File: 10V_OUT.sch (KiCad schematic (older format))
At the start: 7 parts, among them U1 LM321

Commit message: Comments and Notation for clarity
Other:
- note added: "2nd Order Low Pass Filter"
- note added: "Non-Inverting Amplifier"
- moved on the sheet: R3, R4, U1
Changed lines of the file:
@@
 L Amplifier_Operational:LM321 U1
 U 1 1 60A73539
-P 6850 3450
-F 0 "U1" H 7194 3496 50  0000 L CNN
-F 1 "LM321" H 7194 3405 50  0000 L CNN
-F 2 "Package_TO_SOT_SMD:SOT-23-5" H 6850 3450 50  0001 C CNN
-F 3 "http://www.ti.com/lit/ds/symlink/lm321.pdf" H 6850 3450 50  0001 C CNN
-	1    6850 3450
+P 7150 3450
+F 0 "U1" H 7250 3350 50  0000 L CNN
+F 1 "LM321" H 7250 3250 50  0000 L CNN
+F 2 "Package_TO_SOT_SMD:SOT-23-5" H 7150 3450 50  0001 C CNN
+F 3 "http://www.ti.com/lit/ds/symlink/lm321.pdf" H 7150 3450 50  0001 C CNN
+	1    7150 3450
 	1    0    0    -1
 $EndComp
@@
 L Device:R_US R4
 U 1 1 60A77E98
-P 6800 4350
-F 0 "R4" V 6595 4350 50  0000 C CNN
-F 1 "22k" V 6686 4350 50  0000 C CNN
-F 2 "" V 6840 4340 50  0001 C CNN
-F 3 "~" H 6800 4350 50  0001 C CNN
-	1    6800 4350
+P 7100 4350
+F 0 "R4" V 6895 4350 50  0000 C CNN
+F 1 "22k" V 6986 4350 50  0000 C CNN
+F 2 "" V 7140 4340 50  0001 C CNN
+F 3 "~" H 7100 4350 50  0001 C CNN
+	1    7100 4350
 	0    1    1    0
 $EndComp
@@
 L Device:R_US R3
 U 1 1 60A78F26
-P 6300 4350
-F 0 "R3" V 6095 4350 50  0000 C CNN
-F 1 "10k" V 6186 4350 50  0000 C CNN
-F 2 "" V 6340 4340 50  0001 C CNN
-F 3 "~" H 6300 4350 50  0001 C CNN
-	1    6300 4350
+P 6600 4350
+F 0 "R3" V 6395 4350 50  0000 C CNN
+F 1 "10k" V 6486 4350 50  0000 C CNN
+F 2 "" V 6640 4340 50  0001 C CNN
+F 3 "~" H 6600 4350 50  0001 C CNN
+	1    6600 4350
 	0    1    1    0
 $EndComp
@@
 	5950 3350 5950 3550
 Wire Wire Line
-	5950 3350 6550 3350
-Connection ~ 5950 3350
+	7450 3450 7600 3450
 Wire Wire Line
-	7150 3450 7300 3450
+	7600 3450 7600 4350
 Wire Wire Line
-	7300 3450 7300 4350
+	7600 4350 7250 4350
 Wire Wire Line
-	7300 4350 6950 4350
+	6950 4350 6850 4350
 Wire Wire Line
-	6650 4350 6550 4350
+	6850 3550 6850 4350
+Connection ~ 6850 4350
 Wire Wire Line
-	6550 3550 6550 4350
-Connection ~ 6550 4350
-Wire Wire Line
-	6550 4350 6450 4350
-Wire Wire Line
-	6150 4350 5950 4350
+	6850 4350 6750 4350
 Wire Wire Line
 	5250 4050 5250 4350
@@
 Wire Wire Line
 	5950 4050 5950 4350
+Wire Wire Line
+	5950 4350 5250 4350
+Text HLabel 7950 3450 2    50   Input ~ 0
+OUT
+Wire Wire Line
+	7600 3450 7950 3450
+Connection ~ 7600 3450
+Text GLabel 7250 3900 2    50   Input ~ 0
+GND
+Wire Wire Line
+	7050 3750 7050 3900
+Wire Wire Line
+	7050 3900 7250 3900
+Text GLabel 7250 3000 2    50   Input ~ 0
+24V
+Wire Wire Line
+	7050 3150 7050 3000
+Wire Wire Line
+	7050 3000 7250 3000
+Wire Wire Line
+	5950 4350 6450 4350
 Connection ~ 5950 4350
 Wire Wire Line
-	5950 4350 5250 4350
-Text HLabel 7650 3450 2    50   Input ~ 0
-OUT
-Wire Wire Line
-	7300 3450 7650 3450
-Connection ~ 7300 3450
-Text GLabel 6950 3900 2    50   Input ~ 0
-GND
-Wire Wire Line
-	6750 3750 6750 3900
-Wire Wire Line
-	6750 3900 6950 3900
-Text GLabel 6950 3000 2    50   Input ~ 0
-24V
-Wire Wire Line
-	6750 3150 6750 3000
-Wire Wire Line
-	6750 3000 6950 3000
+	6850 3350 5950 3350
+Connection ~ 5950 3350
+Wire Notes Line
+	4650 3100 6400 3100
+Wire Notes Line
+	6400 3100 6400 4450
+Wire Notes Line
+	6400 4450 4650 4450
+Wire Notes Line
+	4650 4450 4650 3100
+Text Notes 5050 4550 0    50   ~ 0
+2nd Order Low Pass Filter
+Wire Notes Line
+	6450 2900 7750 2900
+Wire Notes Line
+	7750 2900 7750 4450
+Wire Notes Line
+	7750 4450 6450 4450
+Wire Notes Line
+	6450 4450 6450 2900
+Text Notes 6650 4550 0    50   ~ 0
+Non-Inverting Amplifier
 $EndSCHEMATC

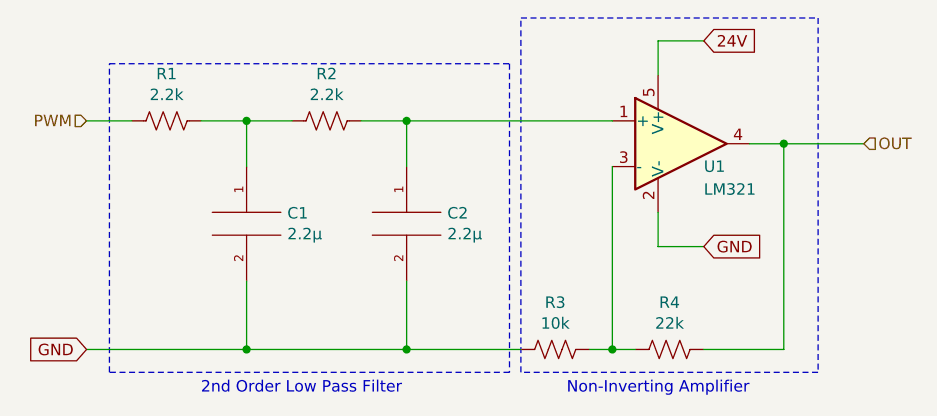
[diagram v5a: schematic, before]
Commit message: Footprint Association
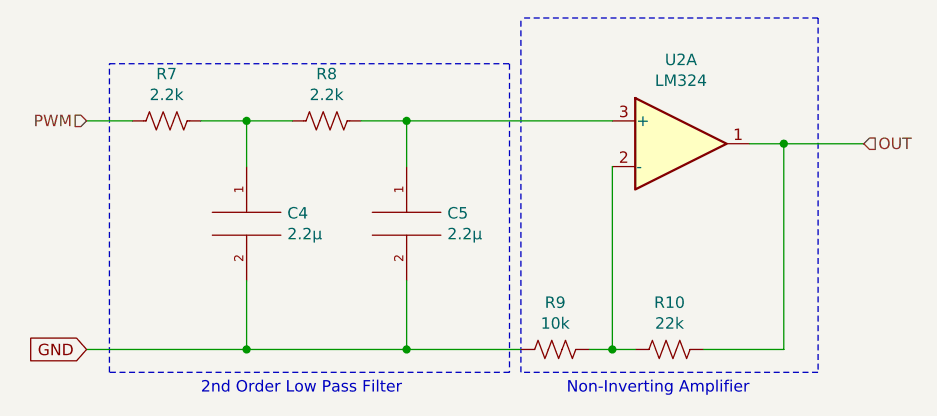
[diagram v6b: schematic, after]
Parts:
- removed U1: LM321, Package_TO_SOT_SMD:SOT-23-5, symbol Amplifier_Operational:LM321
- added U2: LM324, Package_DIP:DIP-14_W7.62mm, symbol Amplifier_Operational:LM324
- C4: renamed from C1; footprint (none) -> Capacitor_THT:C_Disc_D5.1mm_W3.2mm_P5.00mm
- C5: renamed from C2; footprint (none) -> Capacitor_THT:C_Disc_D5.1mm_W3.2mm_P5.00mm
- R10: renamed from R4; footprint (none) -> Resistor_THT:R_Axial_DIN0207_L6.3mm_D2.5mm_P10.16mm_Horizontal
- R7: renamed from R1; footprint (none) -> Resistor_THT:R_Axial_DIN0207_L6.3mm_D2.5mm_P10.16mm_Horizontal
- R8: renamed from R2; footprint (none) -> Resistor_THT:R_Axial_DIN0207_L6.3mm_D2.5mm_P10.16mm_Horizontal
- R9: renamed from R3; footprint (none) -> Resistor_THT:R_Axial_DIN0207_L6.3mm_D2.5mm_P10.16mm_Horizontal
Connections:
- net OUT: now also U2.1
- net at C5.1, R8.1: now also U2.3 (+)
- net at R10.2, R9.1: now also U2.2 (-)
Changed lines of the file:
@@
 $EndDescr
 $Comp
-L Device:R_US R1
+L Device:R_US R7
 U 1 1 60A68EC1
 P 4900 3350
-F 0 "R1" V 4695 3350 50  0000 C CNN
+F 0 "R7" V 4695 3350 50  0000 C CNN
 F 1 "2.2k" V 4786 3350 50  0000 C CNN
-F 2 "" V 4940 3340 50  0001 C CNN
+F 2 "Resistor_THT:R_Axial_DIN0207_L6.3mm_D2.5mm_P10.16mm_Horizontal" V 4940 3340 50  0001 C CNN
 F 3 "~" H 4900 3350 50  0001 C CNN
 	1    4900 3350
@@
 PWM
 $Comp
-L pspice:CAP C1
+L pspice:CAP C4
 U 1 1 60A6A595
 P 5250 3800
-F 0 "C1" H 5428 3846 50  0000 L CNN
+F 0 "C4" H 5428 3846 50  0000 L CNN
 F 1 "2.2μ" H 5428 3755 50  0000 L CNN
-F 2 "" H 5250 3800 50  0001 C CNN
+F 2 "Capacitor_THT:C_Disc_D5.1mm_W3.2mm_P5.00mm" H 5250 3800 50  0001 C CNN
 F 3 "~" H 5250 3800 50  0001 C CNN
 	1    5250 3800
@@
 $EndComp
 $Comp
-L Device:R_US R2
+L Device:R_US R8
 U 1 1 60A6E48F
 P 5600 3350
-F 0 "R2" V 5395 3350 50  0000 C CNN
+F 0 "R8" V 5395 3350 50  0000 C CNN
 F 1 "2.2k" V 5486 3350 50  0000 C CNN
-F 2 "" V 5640 3340 50  0001 C CNN
+F 2 "Resistor_THT:R_Axial_DIN0207_L6.3mm_D2.5mm_P10.16mm_Horizontal" V 5640 3340 50  0001 C CNN
 F 3 "~" H 5600 3350 50  0001 C CNN
 	1    5600 3350
@@
 $EndComp
 $Comp
-L pspice:CAP C2
+L pspice:CAP C5
 U 1 1 60A6E495
 P 5950 3800
-F 0 "C2" H 6128 3846 50  0000 L CNN
+F 0 "C5" H 6128 3846 50  0000 L CNN
 F 1 "2.2μ" H 6128 3755 50  0000 L CNN
-F 2 "" H 5950 3800 50  0001 C CNN
+F 2 "Capacitor_THT:C_Disc_D5.1mm_W3.2mm_P5.00mm" H 5950 3800 50  0001 C CNN
 F 3 "~" H 5950 3800 50  0001 C CNN
 	1    5950 3800
@@
 GND
 $Comp
-L Amplifier_Operational:LM321 U1
-U 1 1 60A73539
-P 7150 3450
-F 0 "U1" H 7250 3350 50  0000 L CNN
-F 1 "LM321" H 7250 3250 50  0000 L CNN
-F 2 "Package_TO_SOT_SMD:SOT-23-5" H 7150 3450 50  0001 C CNN
-F 3 "http://www.ti.com/lit/ds/symlink/lm321.pdf" H 7150 3450 50  0001 C CNN
-	1    7150 3450
-	1    0    0    -1
-$EndComp
-$Comp
-L Device:R_US R4
+L Device:R_US R10
 U 1 1 60A77E98
 P 7100 4350
-F 0 "R4" V 6895 4350 50  0000 C CNN
+F 0 "R10" V 6895 4350 50  0000 C CNN
 F 1 "22k" V 6986 4350 50  0000 C CNN
-F 2 "" V 7140 4340 50  0001 C CNN
+F 2 "Resistor_THT:R_Axial_DIN0207_L6.3mm_D2.5mm_P10.16mm_Horizontal" V 7140 4340 50  0001 C CNN
 F 3 "~" H 7100 4350 50  0001 C CNN
 	1    7100 4350
@@
 $EndComp
 $Comp
-L Device:R_US R3
+L Device:R_US R9
 U 1 1 60A78F26
 P 6600 4350
-F 0 "R3" V 6395 4350 50  0000 C CNN
+F 0 "R9" V 6395 4350 50  0000 C CNN
 F 1 "10k" V 6486 4350 50  0000 C CNN
-F 2 "" V 6640 4340 50  0001 C CNN
+F 2 "Resistor_THT:R_Axial_DIN0207_L6.3mm_D2.5mm_P10.16mm_Horizontal" V 6640 4340 50  0001 C CNN
 F 3 "~" H 6600 4350 50  0001 C CNN
 	1    6600 4350
@@
 	7600 3450 7950 3450
 Connection ~ 7600 3450
-Text GLabel 7250 3900 2    50   Input ~ 0
-GND
-Wire Wire Line
-	7050 3750 7050 3900
-Wire Wire Line
-	7050 3900 7250 3900
-Text GLabel 7250 3000 2    50   Input ~ 0
-24V
-Wire Wire Line
-	7050 3150 7050 3000
-Wire Wire Line
-	7050 3000 7250 3000
 Wire Wire Line
 	5950 4350 6450 4350
@@
 2nd Order Low Pass Filter
 Wire Notes Line
-	6450 2900 7750 2900
-Wire Notes Line
 	7750 2900 7750 4450
 Wire Notes Line
@@
 Text Notes 6650 4550 0    50   ~ 0
 Non-Inverting Amplifier
+Wire Notes Line
+	7750 2900 6450 2900
+$Comp
+L Amplifier_Operational:LM324 U2
+U 1 1 60C64EB2
+P 7150 3450
+F 0 "U2" H 7150 3817 50  0000 C CNN
+F 1 "LM324" H 7150 3726 50  0000 C CNN
+F 2 "Package_DIP:DIP-14_W7.62mm" H 7100 3550 50  0001 C CNN
+F 3 "http://www.ti.com/lit/ds/symlink/lm2902-n.pdf" H 7200 3650 50  0001 C CNN
+	1    7150 3450
+	1    0    0    -1
+$EndComp
 $EndSCHEMATC

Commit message: Finished 1st revision of 24V digital output circuit
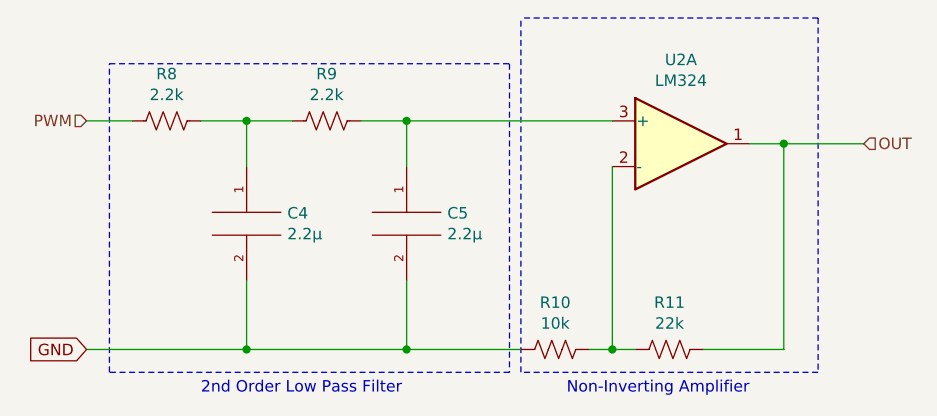
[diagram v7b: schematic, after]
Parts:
- renumbered R9 to R10, R10 to R11, R7 to R8, R8 to R9
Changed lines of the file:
@@
 $EndDescr
 $Comp
-L Device:R_US R7
+L Device:R_US R8
 U 1 1 60A68EC1
 P 4900 3350
-F 0 "R7" V 4695 3350 50  0000 C CNN
+F 0 "R8" V 4695 3350 50  0000 C CNN
 F 1 "2.2k" V 4786 3350 50  0000 C CNN
 F 2 "Resistor_THT:R_Axial_DIN0207_L6.3mm_D2.5mm_P10.16mm_Horizontal" V 4940 3340 50  0001 C CNN
@@
 $EndComp
 $Comp
-L Device:R_US R8
+L Device:R_US R9
 U 1 1 60A6E48F
 P 5600 3350
-F 0 "R8" V 5395 3350 50  0000 C CNN
+F 0 "R9" V 5395 3350 50  0000 C CNN
 F 1 "2.2k" V 5486 3350 50  0000 C CNN
 F 2 "Resistor_THT:R_Axial_DIN0207_L6.3mm_D2.5mm_P10.16mm_Horizontal" V 5640 3340 50  0001 C CNN
@@
 GND
 $Comp
-L Device:R_US R10
+L Device:R_US R11
 U 1 1 60A77E98
 P 7100 4350
-F 0 "R10" V 6895 4350 50  0000 C CNN
+F 0 "R11" V 6895 4350 50  0000 C CNN
 F 1 "22k" V 6986 4350 50  0000 C CNN
 F 2 "Resistor_THT:R_Axial_DIN0207_L6.3mm_D2.5mm_P10.16mm_Horizontal" V 7140 4340 50  0001 C CNN
@@
 $EndComp
 $Comp
-L Device:R_US R9
+L Device:R_US R10
 U 1 1 60A78F26
 P 6600 4350
-F 0 "R9" V 6395 4350 50  0000 C CNN
+F 0 "R10" V 6395 4350 50  0000 C CNN
 F 1 "10k" V 6486 4350 50  0000 C CNN
 F 2 "Resistor_THT:R_Axial_DIN0207_L6.3mm_D2.5mm_P10.16mm_Horizontal" V 6640 4340 50  0001 C CNN
